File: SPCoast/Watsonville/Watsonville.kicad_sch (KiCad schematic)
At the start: 127 parts, among them SW11 11, SW13 13, SW15 15, SW17 17, SW19 19, SW21 21, SW23 23, SW25 25, SW3 3, SW5 5, SW7 7, SW837 837, SW9 9

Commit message: SPCoast: owner's edits: NextCP names, Christopher heads and masts, Sargent milepost, Watsonville circuits and desk tokens (baseline)
- NextCP values name interlockings: GilroyCalTrain CP2 -> Gilroy Interchange;
  Luchessa CP1 -> Gilroy Interchange, CP2 -> Hollister, CP3 and CP4 ->
  Christopher.
- Christopher: the two unnamed dwarf masts, their IRJ-Signals (now plain IRJs)
  and heads removed; remaining heads lettered A, B, C.
- Sargent MAIN HOUSE Milepost 83.5.
- Watsonville circuits SDT -> 0DT and SAT -> 0AT; desk tokens 0DT, 0AT, AT and
  Watsonville:837T1 follow.

Verified: netlists rebuild (Christopher 30, Corporal 27, GilroyCalTrain 28,
GilroyInterchange 23, Luchessa 35, Sargent 19, Watsonville 97, South-cTc 341);
Christopher has no mast or head diagnostics left; desk compiles to 75
appliances, 137 bindings, 14 columns; no root-UUID regression.

Co-Authored-By: Claude Sonnet 5.5 <noreply@anthropic.com>
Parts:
- TC2: value SAT -> 0AT
- TC3: value SDT -> 0DT
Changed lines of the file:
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@@
 			)
 		)
-		(property "Value" "SDT"
+		(property "Value" "0DT"
 			(at 51.31 70.87 0)
 			(show_name no)
@@
 			)
 		)
-		(property "Value" "SAT"
+		(property "Value" "0AT"
 			(at 66.55 101.35 0)
 			(show_name no)

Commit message: SPCoast: owner's edits: Watsonville virtual indications 0100T and 0101T, circuits 01T..03T, desk tokens (baseline)
Includes typos in the member lists (a period for a comma, a missing 25T1, a stray 03T), corrected in the next commit.

Co-Authored-By: Claude Sonnet 5.5 <noreply@anthropic.com>
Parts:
- added TC32: 0100T, symbol Railroad:Virtual Indication
- added TC34: 0101T, symbol Railroad:Virtual Indication
- TC1: value AT -> 01T
- TC2: value 0AT -> 02T
- TC3: value 0DT -> 03T

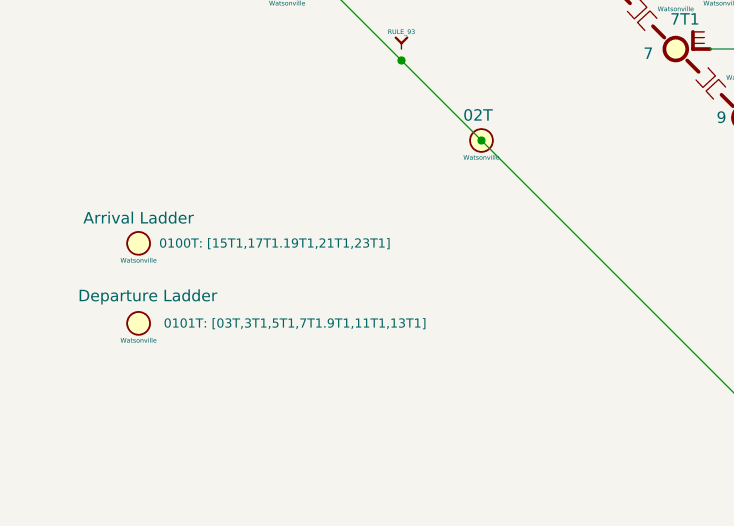
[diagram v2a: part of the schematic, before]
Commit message: fix(kicad): Watsonville virtual indication member lists match the owner's definition
0100T lists 15T1, 17T1, 19T1, 21T1, 23T1, 25T1 (period fixed to comma, 25T1 added).
0101T lists 3T1, 5T1, 7T1, 9T1, 11T1, 13T1 (period fixed, stray 03T removed).

Verified: every member resolves to a Watsonville switch OS circuit; netlist 99 nets.

Co-Authored-By: Claude Sonnet 5.5 <noreply@anthropic.com>
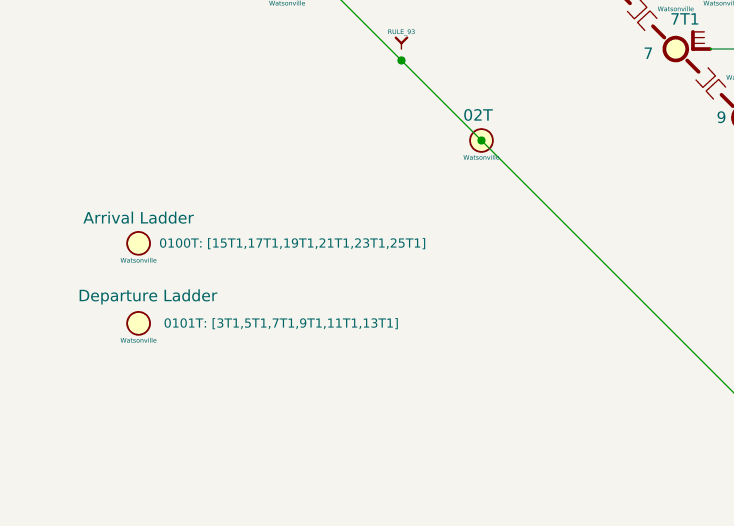
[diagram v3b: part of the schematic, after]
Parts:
- TC32: IndicationToken 15T1,17T1.19T1,21T1,23T1 -> 15T1,17T1,19T1,21T1,23T1,25T1
- TC34: IndicationToken 03T,3T1,5T1,7T1.9T1,11T1,13T1 -> 3T1,5T1,7T1,9T1,11T1,13T1
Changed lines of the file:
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@@
 			)
 		)
-		(property "IndicationToken" "15T1,17T1.19T1,21T1,23T1"
+		(property "IndicationToken" "15T1,17T1,19T1,21T1,23T1,25T1"
 			(at 24.638 119.634 0)
 			(hide yes)
@@
 			)
 		)
-		(property "IndicationToken" "03T,3T1,5T1,7T1.9T1,11T1,13T1"
+		(property "IndicationToken" "3T1,5T1,7T1,9T1,11T1,13T1"
 			(at 24.638 128.524 0)
 			(hide yes)

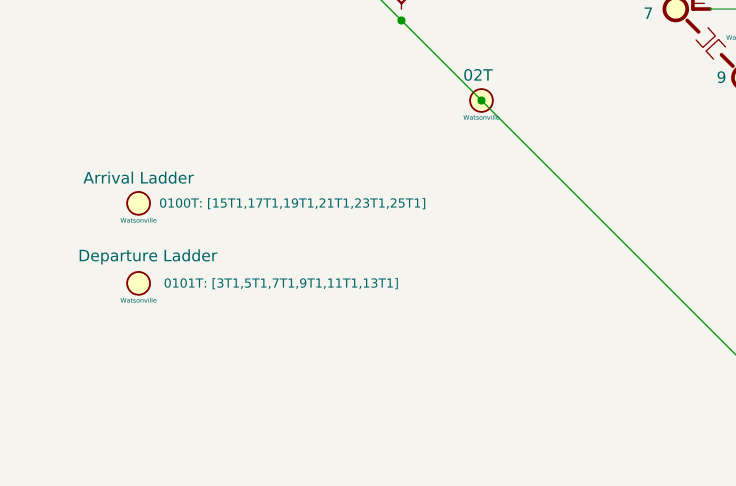
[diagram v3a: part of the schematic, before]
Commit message: SPCoast: owner's edits: 03T in 0101T, South-cTc sheet file renamed GilroyCaltrain.kicad_sch (baseline)
The rename changes only letter case, which git on a case-insensitive filesystem does not see; the index entry was replaced explicitly. The sheet name still contains a typo (Caltain), fixed next.

Co-Authored-By: Claude Sonnet 5.5 <noreply@anthropic.com>
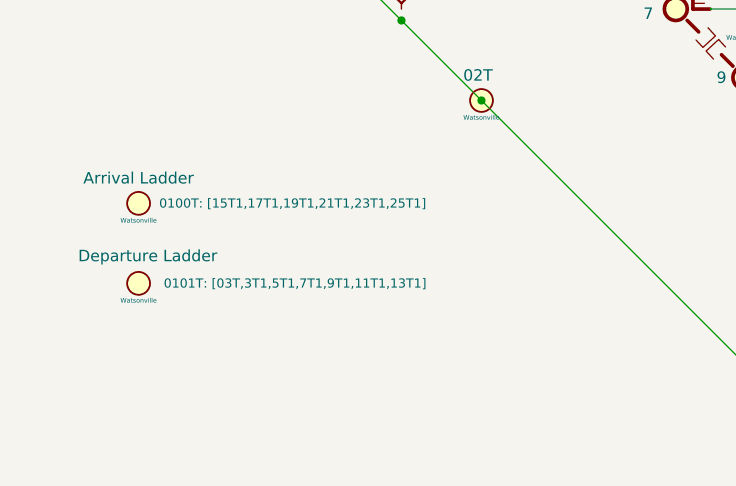
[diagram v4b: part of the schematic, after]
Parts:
- TC34: IndicationToken 3T1,5T1,7T1,9T1,11T1,13T1 -> 03T,3T1,5T1,7T1,9T1,11T1,13T1
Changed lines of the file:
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@@
 			)
 		)
-		(property "IndicationToken" "3T1,5T1,7T1,9T1,11T1,13T1"
+		(property "IndicationToken" "03T,3T1,5T1,7T1,9T1,11T1,13T1"
 			(at 24.638 128.524 0)
 			(hide yes)

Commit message: chore(kicad): refresh instances to the ADR 0003 libraries (InterlockingPlant 95f53e2)
- Desk sheets (South-cTc/*) and the Sargent sandbox: embedded PanelSwitch, PanelLock,
  PanelSignal, PanelMCall, PanelCode, PanelLamp-*, PanelColumn-MAX7313 definitions refreshed
  from the library (refresh_embedded.py, checked against the pre-pass library: only Description
  text had drifted). Instance Role APPLIANCE -> PANEL (77).
- Plant sheets: powered-switch instance Kind SWITCH_POWERED -> SWITCH_REMOTE (21), matching the
  library (sweep_role_kind_fields.py).

Verified:
- verify_symbol_diff.py: same symbols, lib_ids and positions; only Role/Kind changed.
- Nets unchanged: Christopher 30, Corporal 27, GilroyCalTrain 28, GilroyInterchange 23,
  Luchessa 35, Sargent 61, Watsonville 99, South-cTc 341.
- parse_kicad_plant.py --format text identical before/after for all seven plants.
- Desk compile 75/137/14, diagnostics identical; the 7 desk locks bind WLS/~{WLS}/~{WLK}/WLK
  to the bits that were NWS/RWS/RWK/NWK.
- No sheet or project outside Luchessa carries the copied root UUID.

Co-Authored-By: Claude Opus 5.5 <noreply@anthropic.com>
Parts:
- SW11, SW13, SW15, SW17, SW19, SW21, SW23, SW25, SW3, SW5, SW7, SW837, SW9: Kind SWITCH_POWERED -> SWITCH_REMOTE
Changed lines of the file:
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@@
 			)
 		)
-		(property "Kind" "SWITCH_POWERED"
+		(property "Kind" "SWITCH_REMOTE"
 			(at 222.885 87.63 0)
 			(hide yes)
@@
 			)
 		)
-		(property "Kind" "SWITCH_POWERED"
+		(property "Kind" "SWITCH_REMOTE"
 			(at 69.85 73.66 0)
 			(hide yes)
@@
 			)
 		)
-		(property "Kind" "SWITCH_POWERED"
+		(property "Kind" "SWITCH_REMOTE"
 			(at 238.125 102.87 0)
 			(hide yes)
@@
 			)
 		)
-		(property "Kind" "SWITCH_POWERED"
+		(property "Kind" "SWITCH_REMOTE"
 			(at 83.185 92.71 0)
 			(hide yes)
@@
 			)
 		)
-		(property "Kind" "SWITCH_POWERED"
+		(property "Kind" "SWITCH_REMOTE"
 			(at 113.665 123.19 0)
 			(hide yes)
@@
 			)
 		)
-		(property "Kind" "SWITCH_POWERED"
+		(property "Kind" "SWITCH_REMOTE"
 			(at 98.425 107.95 0)
 			(hide yes)
@@
 			)
 		)
-		(property "Kind" "SWITCH_POWERED"
+		(property "Kind" "SWITCH_REMOTE"
 			(at 230.505 95.25 0)
 			(hide yes)
@@
 			)
 		)
-		(property "Kind" "SWITCH_POWERED"
+		(property "Kind" "SWITCH_REMOTE"
 			(at 90.805 100.33 0)
 			(hide yes)
@@
 			)
 		)
-		(property "Kind" "SWITCH_POWERED"
+		(property "Kind" "SWITCH_REMOTE"
 			(at 253.365 118.11 0)
 			(hide yes)
@@
 			)
 		)
-		(property "Kind" "SWITCH_POWERED"
+		(property "Kind" "SWITCH_REMOTE"
 			(at 245.745 110.49 0)
 			(hide yes)
@@
 			)
 		)
-		(property "Kind" "SWITCH_POWERED"
+		(property "Kind" "SWITCH_REMOTE"
 			(at 29.21 73.66 0)
 			(hide yes)
@@
 			)
 		)
-		(property "Kind" "SWITCH_POWERED"
+		(property "Kind" "SWITCH_REMOTE"
 			(at 190.5 86.36 0)
 			(hide yes)
@@
 			)
 		)
-		(property "Kind" "SWITCH_POWERED"
+		(property "Kind" "SWITCH_REMOTE"
 			(at 106.045 115.57 0)
 			(hide yes)
